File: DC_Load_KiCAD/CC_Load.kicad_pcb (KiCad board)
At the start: 2 copper layers, 120 x 62 mm, 65 parts, among them J1 VoltSense_Conn, J2 PowerInput_Conn, J3 LED_Conn, J4 Load_Conn, J5 16x2_LCD_Conn, J6 RotEnc_Conn, J7 Fan_Conn, Q1 IRLZ44N, Q2 IRLZ44N, Q3 IRLZ44N, Q4 IRLZ44N, Q5 IRLZ44N, U1 LM7805_TO220, U2 LM358

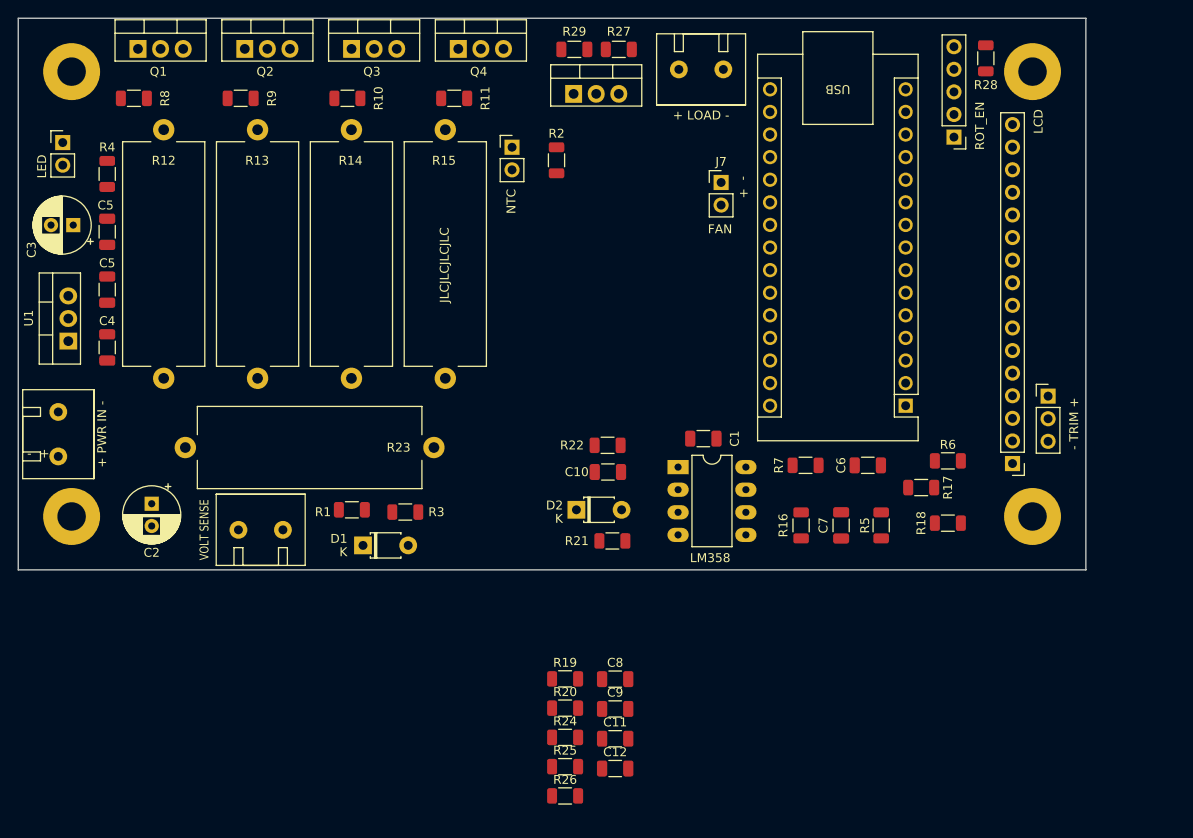
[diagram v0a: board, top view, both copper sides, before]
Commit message: Update PCB and prepare for ordering
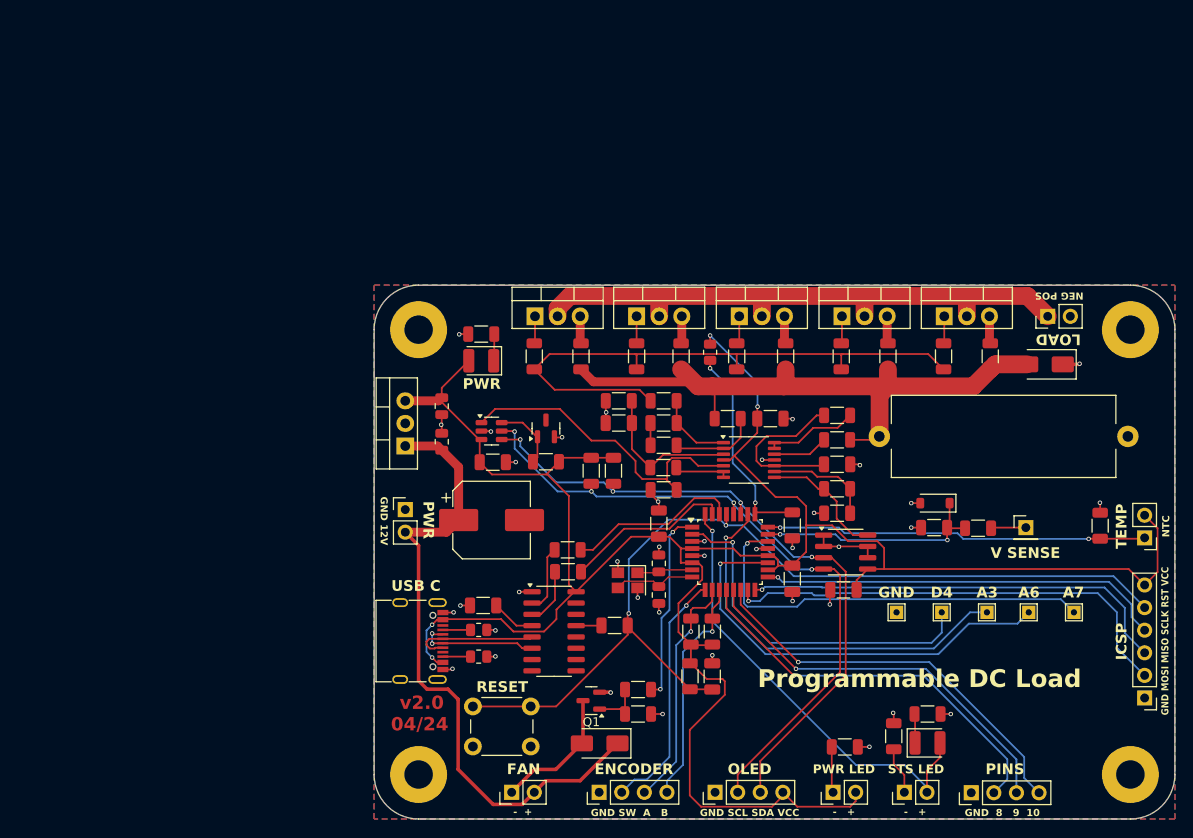
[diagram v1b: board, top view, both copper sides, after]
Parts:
- removed A1: Arduino_Nano, Module:Arduino_Nano
- removed the C5 at (60.0, 54.0)
- removed the C5 at (60.0, 60.5)
- removed RV1: 10k, Connector_PinHeader_2.54mm:PinHeader_1x03_P2.54mm_Vertical
- added C13: 10p, Capacitor_SMD:C_0805_2012Metric, F.Cu at (122.0, 91.3)
- added C14: 10p, Capacitor_SMD:C_0805_2012Metric, F.Cu at (122.0, 94.8)
- added C15: 100n, Capacitor_SMD:C_1206_3216Metric, F.Cu at (142.0, 80.1)
- added C16: 100n, Capacitor_SMD:C_1206_3216Metric, F.Cu at (103.3, 79.9)
- added C5: 22u, Capacitor_SMD:C_0805_2012Metric, F.Cu at (97.6, 73.6)
- added D3: 5V, Diode_SMD:D_SOD-123, F.Cu at (153.0, 84.5)
- added D4: RED, LED_SMD:LED_1210_3225Metric, F.Cu at (152.2, 111.5)
- added D5: SS34, Diode_SMD:D_SMA, F.Cu at (165.4, 68.9)
- added J10: CONN_LED, Connector_PinHeader_2.54mm:PinHeader_1x02_P2.54mm_Vertical, F.Cu at (149.6, 117.0)
- added J11: CONN_ICSP, Connector_PinHeader_2.54mm:PinHeader_1x06_P2.54mm_Vertical, F.Cu at (176.6, 106.4)
- added J12: CONN_PINS, Connector_PinHeader_2.54mm:PinHeader_1x04_P2.54mm_Vertical, F.Cu at (157.1, 117.0)
- added J8: CONN_ENCODER, Connector_PinHeader_2.54mm:PinHeader_1x04_P2.54mm_Vertical, F.Cu at (115.3, 117.0)
- added J9: CONN_OLED, Connector_PinHeader_2.54mm:PinHeader_1x04_P2.54mm_Vertical, F.Cu at (128.3, 117.0)
- added Q6: IRLZ44N, Package_TO_SOT_THT:TO-220-3_Vertical, F.Cu at (154.1, 63.5)
- added R30: 0.2R, Resistor_SMD:R_1206_3216Metric, F.Cu at (124.5, 68.0)
- added R31: 0.2R, Resistor_SMD:R_1206_3216Metric, F.Cu at (136.2, 68.0)
- added R32: 0.2R, Resistor_SMD:R_1206_3216Metric, F.Cu at (147.8, 68.0)
- added R33: 0.2R, Resistor_SMD:R_1206_3216Metric, F.Cu at (159.2, 68.0)
- added R34: 10k, Resistor_SMD:R_1206_3216Metric, F.Cu at (129.7, 75.0)
- added R35: 10k, Resistor_SMD:R_1206_3216Metric, F.Cu at (142.0, 77.4)
- added R36: 100R, Resistor_SMD:R_1206_3216Metric, F.Cu at (142.0, 74.6)
- added R37: 0.1R, Resistor_THT:R_Axial_Power_L25.0mm_W9.0mm_P27.94mm, F.Cu at (146.8, 77.0)
- added R38: 10k, Resistor_SMD:R_1206_3216Metric, F.Cu at (142.0, 82.9)
- added R39: 1k, Resistor_SMD:R_1206_3216Metric, F.Cu at (142.0, 85.6)
- added R40: 1k, Resistor_SMD:R_1206_3216Metric, F.Cu at (109.3, 79.8)
- added R41: 470R, Resistor_SMD:R_1206_3216Metric, F.Cu at (148.4, 110.7)
- added SW1: RST_BTN, Button_Switch_THT:SW_PUSH_6mm, F.Cu at (101.1, 107.3)
- added TP1: ADC_06, TestPoint:TestPoint_THTPad_1.5x1.5mm_Drill0.7mm, F.Cu at (163.6, 96.8)
- added TP2: ADC_07, TestPoint:TestPoint_THTPad_1.5x1.5mm_Drill0.7mm, F.Cu at (168.7, 96.8)
- added TP3: ADC_03, TestPoint:TestPoint_THTPad_1.5x1.5mm_Drill0.7mm, F.Cu at (158.9, 96.8)
- added TP4: PIN_04, TestPoint:TestPoint_THTPad_1.5x1.5mm_Drill0.7mm, F.Cu at (153.8, 96.8)
- added TP5: TP_GND, TestPoint:TestPoint_THTPad_1.5x1.5mm_Drill0.7mm, F.Cu at (148.7, 96.8)
- added U3: CH340C, Package_SO:SOIC-16_3.9x9.9mm_P1.27mm, F.Cu at (110.2, 98.9)
- added U4: ATmega328P-A, Package_QFP:TQFP-32_7x7mm_P0.8mm, F.Cu at (130.0, 90.0)
- added U5: ADC (INA219AIDR), Package_SO:SOIC-8_3.9x4.9mm_P1.27mm, F.Cu at (143.0, 90.0)
- added U6: DAC (MCP4716A0T-E/CH), Package_TO_SOT_SMD:SOT-23-6, F.Cu at (103.2, 76.4)
- added U7: ADR5040BRTZ, Package_TO_SOT_SMD:SOT-23, F.Cu at (109.3, 76.1)
- added Y1: 16MHz, Crystal:Crystal_SMD_3225-4Pin_3.2x2.5mm, F.Cu at (118.5, 93.2)
- C1, C7: value 100nF -> 100n
- C2: value 100uF -> 100n; footprint Capacitor_THT:CP_Radial_D6.3mm_P2.50mm -> Capacitor_SMD:C_1206_3216Metric
- C3: value 100uF -> 100u; footprint Capacitor_THT:CP_Radial_D6.3mm_P2.50mm -> Capacitor_SMD:CP_Elec_8x10.5
- C4: value 100nF -> 22u; footprint Capacitor_SMD:C_1206_3216Metric -> Capacitor_SMD:C_0805_2012Metric
- C6: value 1nF -> 100n
- D1: value 5V -> SS34; footprint Diode_THT:D_T-1_P5.08mm_Horizontal -> Diode_SMD:D_SMA
- D2: value D -> RED; footprint Diode_THT:D_T-1_P5.08mm_Horizontal -> LED_SMD:LED_1210_3225Metric
- H1, H2, H3, H4: value MountingHole_Pad -> MH
- J1: value VoltSense_Conn -> CONN_V_SENSE; footprint MyFootprintLibrary:ScrewTerminal_01x02_P5mm -> Connector_PinHeader_2.54mm:PinHeader_1x01_P2.54mm_Vertical
- J2: value PowerInput_Conn -> CONN_FAN; footprint MyFootprintLibrary:ScrewTerminal_01x02_P5mm -> Connector_PinHeader_2.54mm:PinHeader_1x02_P2.54mm_Vertical
- J3: value LED_Conn -> CONN_PWR
- J4: value Load_Conn -> CONN_PWR_LED; footprint MyFootprintLibrary:ScrewTerminal_01x02_P5mm -> Connector_PinHeader_2.54mm:PinHeader_1x02_P2.54mm_Vertical
- J5: value 16x2_LCD_Conn -> USBC_CONN; footprint Connector_PinHeader_2.54mm:PinHeader_1x16_P2.54mm_Vertical -> Connector_USB:USB_C_Receptacle_G-Switch_GT-USB-7010ASV
- J6: value RotEnc_Conn -> CONN_NTC; footprint Connector_PinHeader_2.54mm:PinHeader_1x05_P2.54mm_Vertical -> Connector_PinHeader_2.54mm:PinHeader_1x02_P2.54mm_Vertical
- J7: value Fan_Conn -> CONN_LOAD
- Q1: value IRLZ44N -> 2N7002; footprint Package_TO_SOT_THT:TO-220-3_Vertical -> Package_TO_SOT_SMD:SOT-23
- R1: value 47k -> 5k1; footprint Resistor_SMD:R_1206_3216Metric -> Resistor_SMD:R_0805_2012Metric
- R10, R9: value 100R -> 10k
- R11, R8: value 100R -> 4k7
- R12, R15: value 0.1R -> 10k; footprint Resistor_THT:R_Axial_Power_L25.0mm_W9.0mm_P27.94mm -> Resistor_SMD:R_1206_3216Metric
- R13, R14: value 0.1R -> 4k7; footprint Resistor_THT:R_Axial_Power_L25.0mm_W9.0mm_P27.94mm -> Resistor_SMD:R_1206_3216Metric
- R19: value 22k -> 4k7
- R2: value 10k -> 470R
- R20: value 10k -> 4k7
- R22, R24: value 1k -> 100R
- R23: value 0.1R -> 100R; footprint Resistor_THT:R_Axial_Power_L25.0mm_W9.0mm_P27.94mm -> Resistor_SMD:R_1206_3216Metric
- R25, R26: value 100k -> 100R
- R27: value 220R -> 1k
- R28: value 10k -> 100R
- R29: value 10k -> 0.2R
- R3: value 10k -> 5k1; footprint Resistor_SMD:R_1206_3216Metric -> Resistor_SMD:R_0805_2012Metric
- R4: value 220R -> 470R
- R5: value 10k -> 47k
- R7: value 100R -> 470R
- TH1: value 10k_NTC -> 10k; footprint Connector_PinHeader_2.54mm:PinHeader_1x02_P2.54mm_Vertical -> Resistor_SMD:R_0805_2012Metric
- U2: value LM358 -> OPA4376; footprint Package_DIP:DIP-8_W7.62mm_LongPads -> Package_SO:TSSOP-14_4.4x5mm_P0.65mm
- moved R12 114.3 mm to (171.6, 87.0), turned to 90 degrees
- moved R9 91.7 mm to (152.9, 87.2), turned to 0 degrees
- moved Q1 89.2 mm to (114.4, 106.7), turned to 180 degrees
- moved R11 87.3 mm to (152.2, 108.2)
- moved J1 86.0 mm to (163.2, 87.2)
- moved J4 82.6 mm to (141.6, 117.0), turned to 90 degrees
- moved R10 76.5 mm to (119.7, 108.2)
- moved J5 70.6 mm to (94.0, 100.0), turned to -90 degrees
- moved C2 70.2 mm to (134.5, 75.0), turned to 0 degrees
- moved R4 68.4 mm to (111.8, 92.2), turned to 180 degrees
- moved R26 65.2 mm to (154.0, 68.0), turned to -90 degrees
- moved J2 64.9 mm to (105.5, 117.0), turned to 90 degrees
- moved C3 57.5 mm to (103.2, 86.4), turned to 0 degrees
- moved J3 56.4 mm to (93.5, 85.2)
- moved R25 55.6 mm to (142.5, 68.0), turned to -90 degrees
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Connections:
- C1 pad 1: +5V -> GND
- C1 pad 2: GND -> Net-(U3-V3)
- C10 pad 1: curr_sense -> RST_UC
- C11 pad 2: GND -> Net-(C11-Pad2)
- C12 pad 1: curr_set -> +5V
- C2 pad 1: +12V -> +5V
- C3 pad 1: +5V -> +12V
- C6 pad 1: Net-(C6-Pad1) -> Net-(U3-~{DTR})
- C6 pad 2: Net-(C6-Pad2) -> RST_UC
- C7 pad 1: Net-(U2B-+) -> +5V
- C8 pad 1: Net-(U2A-+) -> +5V
- C9 pad 1: Net-(C9-Pad1) -> CURR_SET_OPAMP
- D1 pad 1: volt_sense -> +12V
- D1 pad 2: GND -> /FAN_NEG
- D2 pad 1: GND -> Net-(D2-K)
- D2 pad 2: Net-(D2-A) -> +5V
- J2 pad 1: GND -> /FAN_NEG
- J3 pad 1: Net-(J3-Pin_1) -> GND
- J3 pad 2: +5V -> +12V
- J4 pad 1: GND -> /PWR_LED_K
- J4 pad 2: Net-(J4-Pin_2) -> +5V
- J6 pad 1: Net-(A1-D9) -> TEMP_SENSE_UC
- J6 pad 2: GND -> +5V
- J7 pad 1: Net-(J7-Pin_1) -> /LOAD_POS
- J7 pad 2: +12V -> GND
- Q1 pad 1: Net-(Q1-G) -> /FAN_OUT_GATE
- Q1 pad 2: Net-(J4-Pin_2) -> GND
- Q1 pad 3: Net-(Q1-S) -> /FAN_NEG
- Q2 pad 2: Net-(J4-Pin_2) -> /LOAD_POS
- Q3 pad 2: Net-(J4-Pin_2) -> /LOAD_POS
- Q4 pad 2: Net-(J4-Pin_2) -> /LOAD_POS
- Q5 pad 2: Net-(J7-Pin_1) -> /LOAD_POS
- Q5 pad 3: GND -> Net-(Q5-S)
- R1 pad 1: volt_sense -> GND
- R1 pad 2: Net-(J1-Pin_1) -> Net-(J5-CC1)
- R10 pad 1: Net-(Q3-G) -> GND
- R10 pad 2: Net-(R10-Pad2) -> /FAN_OUT_GATE
- R11 pad 1: Net-(Q4-G) -> GND
- R11 pad 2: Net-(R10-Pad2) -> Net-(D4-K)
- R12 pad 1: Net-(Q1-S) -> TEMP_SENSE_UC
- R12 pad 2: Net-(D2-A) -> GND
- R13 pad 1: Net-(Q2-S) -> I2C_SCL
- R13 pad 2: Net-(D2-A) -> +5V
- R14 pad 1: Net-(Q3-S) -> I2C_SDA
- R14 pad 2: Net-(D2-A) -> +5V
- R15 pad 1: Net-(Q4-S) -> Net-(U2B--)
- R15 pad 2: Net-(D2-A) -> CURR_SET_OPAMP
- R16 pad 1: GND -> CURR_SET_UC
- R16 pad 2: Net-(U2B-+) -> GND
- R17 pad 1: Net-(U2B--) -> CURR_SET_OPAMP
- R17 pad 2: Net-(C6-Pad2) -> GND
- R18 pad 1: Net-(D2-A) -> SHUNT_TEMP_UC
- R18 pad 2: Net-(U2B--) -> GND
- R19 pad 1: Net-(R19-Pad1) -> ENCODER_B
- R19 pad 2: Net-(U2A--) -> +5V
- R2 pad 1: temp_sense -> RXD_UC
- R2 pad 2: GND -> Net-(U3-TXD)
- R20 pad 1: Net-(U2A-+) -> ENCODER_A
- R20 pad 2: Net-(C9-Pad1) -> +5V
- R21 pad 1: Net-(C9-Pad1) -> RST_UC
- R21 pad 2: Net-(D2-A) -> +5V
- R22 pad 1: curr_sense -> Net-(Q2-G)
- R22 pad 2: Net-(R19-Pad1) -> Net-(R22-Pad2)
- R23 pad 1: Net-(D2-A) -> Net-(Q3-G)
- R23 pad 2: GND -> Net-(R22-Pad2)
- R24 pad 1: Net-(U2A--) -> Net-(Q4-G)
- R24 pad 2: GND -> Net-(R22-Pad2)
- R25 pad 1: Net-(A1-MOSI) -> Net-(Q5-G)
- R25 pad 2: Net-(C11-Pad1) -> Net-(R22-Pad2)
- R26 pad 1: Net-(C11-Pad1) -> Net-(Q6-G)
- R26 pad 2: curr_set -> Net-(R22-Pad2)
- R27 pad 1: fan_control -> Net-(U2A--)
- R27 pad 2: Net-(Q5-G) -> Net-(C11-Pad1)
- R28 pad 1: Net-(J6-Pin_4) -> Net-(C11-Pad2)
- R28 pad 2: +5V -> Net-(R22-Pad2)
- R29 pad 1: GND -> Net-(Q2-S)
- R29 pad 2: Net-(Q5-G) -> /CURR_SHUNT
- R3 pad 2: volt_sense -> Net-(J5-CC2)
- R4 pad 1: GND -> TXD_UC
- R4 pad 2: Net-(J3-Pin_1) -> Net-(U3-RXD)
- R5 pad 1: curr_set -> V_SENSE_UC
- R5 pad 2: Net-(U2B-+) -> Net-(J1-Pin_1)
- R6 pad 1: +5V -> /FAN_OUT_GATE
- R6 pad 2: Net-(J5-Pin_2) -> FAN_OUT
- R7 pad 1: Net-(C6-Pad1) -> GND
- R7 pad 2: Net-(R10-Pad2) -> /PWR_LED_K
- R8 pad 1: Net-(Q1-G) -> GND
- R8 pad 2: Net-(R10-Pad2) -> Net-(D2-K)
- R9 pad 1: Net-(Q2-G) -> GND
- R9 pad 2: Net-(R10-Pad2) -> V_SENSE_UC
- TH1 pad 2: temp_sense -> SHUNT_TEMP_UC
- U2 pad 1: Net-(R19-Pad1) -> Net-(C11-Pad2)
- U2 pad 3: Net-(U2A-+) -> CURR_SET_OPAMP
- U2 pad 4: GND -> +5V
- U2 pad 5: Net-(U2B-+) -> CURR_SET_UC
- U2 pad 7: Net-(C6-Pad1) -> Net-(U2B--)
- U2 pad 8: +5V -> /CURR_SENSE_UC
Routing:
- net +5V: track 0.00 -> 258.6 mm, vias 0 -> 4
- net RST_UC: track 0.00 -> 107.1 mm, vias 0 -> 2
- net I2C_SCL: track 0.00 -> 77.4 mm, vias 0 -> 4
- net I2C_SDA: track 0.00 -> 76.4 mm, vias 0 -> 4
- net +12V: track 0.00 -> 72.4 mm
- net /CURR_SHUNT: track 0.00 -> 71.1 mm
- net Net-(R22-Pad2): track 0.00 -> 67.3 mm
- net /LOAD_POS: track 0.00 -> 66.9 mm
- net GND: track 0.00 -> 55.1 mm, vias 0 -> 38
- net SPI_MOSI_UC: track 0.00 -> 52.5 mm, vias 0 -> 1
- net LED_OUT: track 0.00 -> 51.0 mm, vias 0 -> 1
- net /ADC_06: track 0.00 -> 49.2 mm, vias 0 -> 1
- net SPI_MISO_UC: track 0.00 -> 48.7 mm, vias 0 -> 1
- net /ADC_07: track 0.00 -> 47.5 mm, vias 0 -> 1
- net SPI_SCLK_UC: track 0.00 -> 45.7 mm, vias 0 -> 1
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- added copper zone on B.Cu, net GND
- added copper zone on F.Cu, net GND
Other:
- board size 120 x 62 mm -> 90 x 60 mm
- board text added: "04/24"
- board text added: "A3"
- board text added: "A6"
- board text added: "A7"
- board text added: "D4"
- board text added: "ENCODER"
- board text added: "GND"
- board text added: "GND 12V"
- board text added: "GND 8 9 10"
- board text added: "GND MOSI MISO SCLK RST VCC"
- board text added: "GND SCL SDA VCC"
- board text added: "GND SW A B"
- board text added: "ICSP"
- board text added: "LOAD"
- board text added: "NEG POS"
- board text added: "OLED"
- board text added: "PINS"
- board text added: "PWR"
- board text added: "PWR LED"
- board text added: "Programmable DC Load"
- board text added: "RESET"
- board text added: "STS LED"
- board text added: "TEMP"
- board text added: "USB C"
- board text added: "V SENSE"
- board text added: "github.com/AleksaHeler/DC_Load"
- board text added: "v2.0"
- board text removed: "+ LOAD -"
- board text removed: "+ PWR IN -"
- board text removed: "- TRIM +"
- board text removed: "LCD"
- board text removed: "LED"
- board text removed: "LM358"
- board text removed: "ROT_EN"
- board text removed: "VOLT SENSE"
